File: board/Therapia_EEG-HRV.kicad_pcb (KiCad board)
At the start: 4 copper layers, 61.8 x 45 mm, 141 parts, among them J1 USB-C_16P, J2 Header_2x6

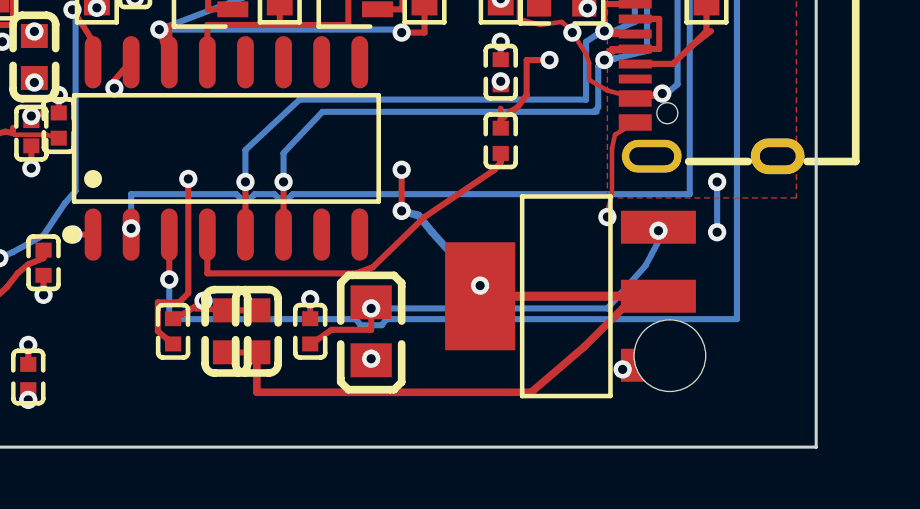
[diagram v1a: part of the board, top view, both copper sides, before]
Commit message: S5 L1: move AMS1117 off mounting hole H4, and fix the identity bug behind it
The regulator's pin 1 (GND) pad had H4's 2.3876 mm drill through its middle.
Moved +3.25/+1.25 mm; every pad now clears the hole by 0.4335 mm against a
0.2 mm rule. West and north -- the ECO's directions -- are blocked: pad 4 runs
into FB3 pin 2 and U_USB pin 8 to the west, and pad 3 into J1 pin 13 and PEG1
to the north. DRC errors 69 -> 59, unconnected 0, contract parity unchanged.

The run also turned up why earlier attempts misbehaved: the EasyEDA importer
gave every instance of a library footprint the same KIID (38 footprints share
one, and their 38 pin-1 pads share another). route.uid() keyed on that alone,
so ignore lists covered parts they never meant to, CopperIndex dropped real
obstacles from queries, and the connectivity check merged 38 unrelated pads --
which is how it called VDD_ESP whole while DRC drew a ratsnest line across it.
uid() now carries the reference and the footprint-relative pad position.

Co-Authored-By: Claude Fable 5 <noreply@anthropic.com>
Claude-Session: https://claude.ai/code/session_01431Pn2abKuPv9KnYCZmkiJ
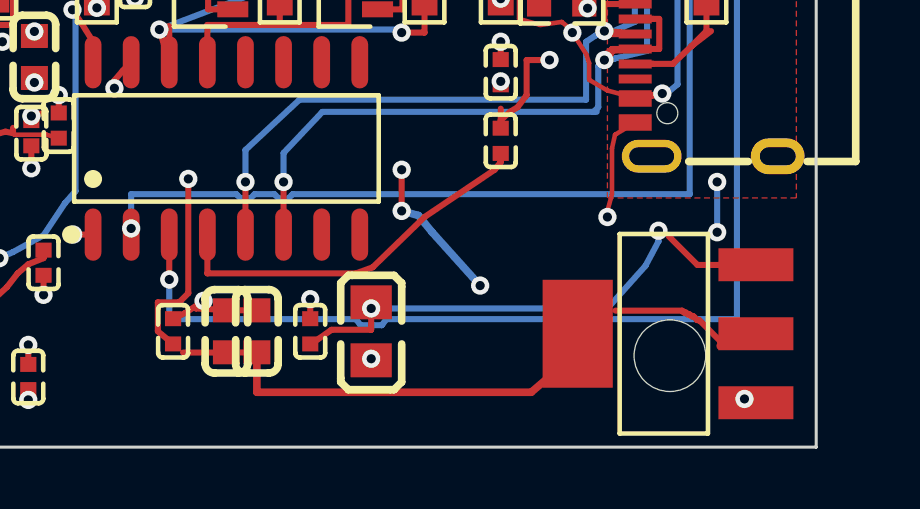
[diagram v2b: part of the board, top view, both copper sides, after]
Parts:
- moved AMS1117 3.48 mm to (176.8, 121.2)
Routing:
- net V_3V3_IN: track 13.7 -> 17.0 mm
- net GND: track 85.8 -> 84.8 mm
- net VDD_ESP: track 37.3 -> 36.6 mm

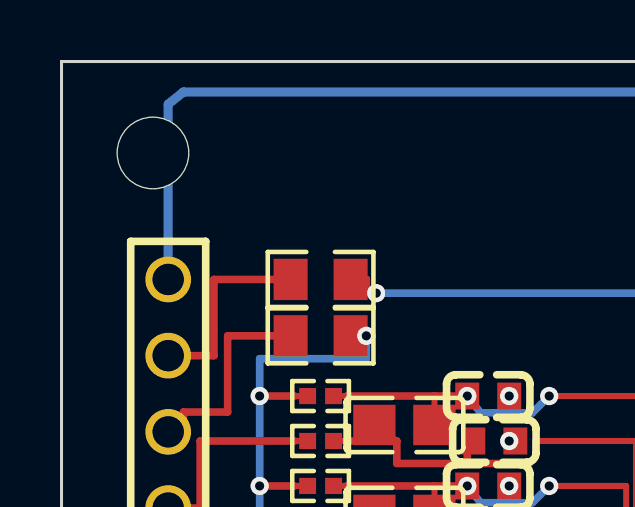
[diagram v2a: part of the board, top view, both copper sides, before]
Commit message: S5 L2: route CHASSIS_GND round mounting hole H1
The bottom-layer shell-ground track from J2 pin 12 ran 0.508 mm from H1's
centre, so the 2.3876 mm drill cut it. Re-routed east of the hole in four
segments, 6.43 mm against 5.84 mm direct, clear by the 0.3 mm target. DRC
errors 59 -> 57, unconnected 0.

The router now string-pulls its result: the first version of this detour came
back as a 25-segment staircase hugging the clearance circle, because an 8-way
grid has many equal-cost paths and A* returns whichever it reached first.

Co-Authored-By: Claude Fable 5 <noreply@anthropic.com>
Claude-Session: https://claude.ai/code/session_01431Pn2abKuPv9KnYCZmkiJ
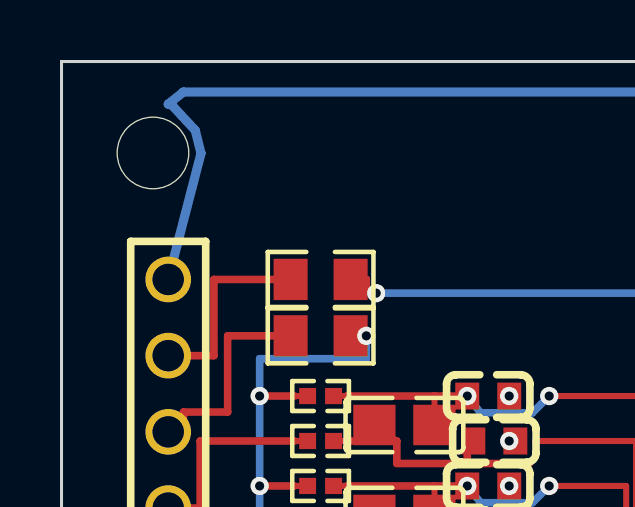
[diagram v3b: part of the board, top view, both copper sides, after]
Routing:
- net CHASSIS_GND: track 88.7 -> 89.3 mm
